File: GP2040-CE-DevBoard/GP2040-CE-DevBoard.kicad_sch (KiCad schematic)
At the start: 0 parts

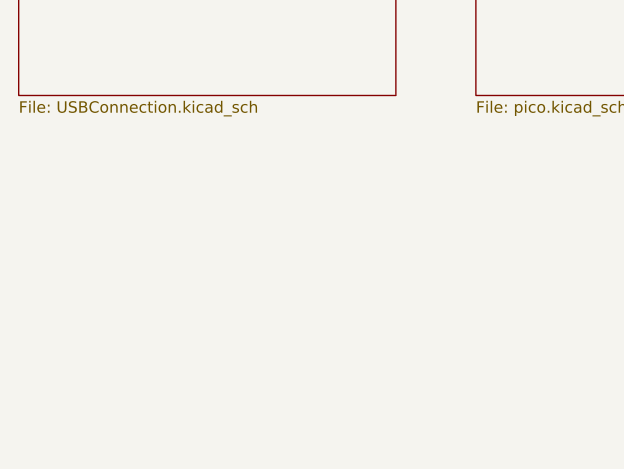
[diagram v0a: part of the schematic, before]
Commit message: Adding Buttons
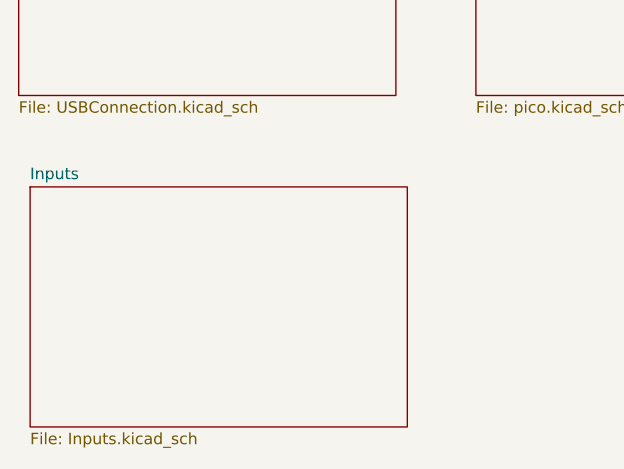
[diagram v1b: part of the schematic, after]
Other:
- added sheet Inputs (Inputs.kicad_sch)
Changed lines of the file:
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@@
+    )
+  )
+  (sheet (at 21.59 59.69) (size 41.91 26.67) (fields_autoplaced)
+    (stroke (width 0.1524) (type solid) (color 0 0 0 0))
+    (fill (color 0 0 0 0.0000))
+    (property "Sheet name" "Inputs" (id 0) (at 21.59 58.9784 0)
+      (effects (font (size 1.27 1.27)) (justify left bottom))
+    )
+    (property "Sheet file" "Inputs.kicad_sch" (id 1) (at 21.59 86.9446 0)
+      (effects (font (size 1.27 1.27)) (justify left top))
     )
   )
@@
     (path "/73fdee15-42f2-4740-b048-36e7f85b9482" (page "3"))
     (path "/b33fe592-84a5-45cc-bdd9-32ad654e4475" (page "4"))
+    (path "/cf4e2c04-ff9e-4c5a-81c6-34ae2464fdd9" (page "5"))
   )
   (symbol_instances
@@
       (reference "#PWR?") (unit 1) (value "GND") (footprint "")
     )
+    (path "/cf4e2c04-ff9e-4c5a-81c6-34ae2464fdd9/49f1f508-92dd-44b5-8cc3-e0cac56a3164"
+      (reference "#PWR?") (unit 1) (value "GND") (footprint "")
+    )
     (path "/b33fe592-84a5-45cc-bdd9-32ad654e4475/4c7c24d6-6d5b-49e6-bf2e-da7d3ae43938"
       (reference "#PWR?") (unit 1) (value "GND") (footprint "")
@@
     )
     (path "/73fdee15-42f2-4740-b048-36e7f85b9482/8d77327b-2bce-4426-8fff-d7f3a5762db8"
+      (reference "#PWR?") (unit 1) (value "GND") (footprint "")
+    )
+    (path "/cf4e2c04-ff9e-4c5a-81c6-34ae2464fdd9/91e16629-9055-4d56-b83e-0a56fc9aee5a"
+      (reference "#PWR?") (unit 1) (value "GND") (footprint "")
+    )
+    (path "/cf4e2c04-ff9e-4c5a-81c6-34ae2464fdd9/9cbedc65-6b48-4c5d-8943-9381607962b6"
       (reference "#PWR?") (unit 1) (value "GND") (footprint "")
     )
@@
       (reference "R?") (unit 1) (value "4.7k") (footprint "Resistor_SMD:R_0805_2012Metric_Pad1.20x1.40mm_HandSolder")
     )
+    (path "/cf4e2c04-ff9e-4c5a-81c6-34ae2464fdd9/0eee3433-e9f7-43cb-b1ae-2be2e9ac6e27"
+      (reference "SW?") (unit 1) (value "SW_Push") (footprint "")
+    )
+    (path "/cf4e2c04-ff9e-4c5a-81c6-34ae2464fdd9/1502c553-9e95-4fe7-a79b-7c0c7eea0150"
+      (reference "SW?") (unit 1) (value "SW_Push") (footprint "")
+    )
+    (path "/cf4e2c04-ff9e-4c5a-81c6-34ae2464fdd9/1ac3d9ce-0481-4d1f-be81-e77269954e3e"
+      (reference "SW?") (unit 1) (value "SW_Push") (footprint "")
+    )
+    (path "/cf4e2c04-ff9e-4c5a-81c6-34ae2464fdd9/24010708-1b23-44d3-b3e1-f95e25bf40d0"
+      (reference "SW?") (unit 1) (value "SW_Push") (footprint "")
+    )
+    (path "/cf4e2c04-ff9e-4c5a-81c6-34ae2464fdd9/31207c80-8b56-4087-bf0b-710dca7763df"
+      (reference "SW?") (unit 1) (value "SW_Push") (footprint "")
+    )
+    (path "/cf4e2c04-ff9e-4c5a-81c6-34ae2464fdd9/3adb4e56-0c30-446e-add9-a441ac4b57cd"
+      (reference "SW?") (unit 1) (value "SW_Push") (footprint "")
+    )
+    (path "/cf4e2c04-ff9e-4c5a-81c6-34ae2464fdd9/42d88e3f-b8f5-411a-b92e-32fb05f43e5f"
+      (reference "SW?") (unit 1) (value "SW_Push") (footprint "")
+    )
+    (path "/cf4e2c04-ff9e-4c5a-81c6-34ae2464fdd9/74ffb43d-c33b-4c8b-abf6-a5ca84fca331"
+      (reference "SW?") (unit 1) (value "SW_Push") (footprint "")
+    )
+    (path "/cf4e2c04-ff9e-4c5a-81c6-34ae2464fdd9/7d9a28b6-31c0-40b8-a6a9-85b90c14eaae"
+      (reference "SW?") (unit 1) (value "SW_Push") (footprint "")
+    )
+    (path "/cf4e2c04-ff9e-4c5a-81c6-34ae2464fdd9/7ee11936-6094-4326-ab0b-c55324458660"
+      (reference "SW?") (unit 1) (value "SW_Push") (footprint "")
+    )
+    (path "/cf4e2c04-ff9e-4c5a-81c6-34ae2464fdd9/8b45d552-607d-4482-8e8b-a9cbdaaf330c"
+      (reference "SW?") (unit 1) (value "SW_Push") (footprint "")
+    )
+    (path "/cf4e2c04-ff9e-4c5a-81c6-34ae2464fdd9/a1ac1f1c-1031-4b49-aaa1-60774ccda8fb"
+      (reference "SW?") (unit 1) (value "SW_Push") (footprint "")
+    )
+    (path "/cf4e2c04-ff9e-4c5a-81c6-34ae2464fdd9/a56d2f31-9696-43af-9213-0c9d4fc4d3b3"
+      (reference "SW?") (unit 1) (value "SW_Push") (footprint "")
+    )
+    (path "/cf4e2c04-ff9e-4c5a-81c6-34ae2464fdd9/a8c128d9-41bc-47f7-bc55-25fd741f1723"
+      (reference "SW?") (unit 1) (value "SW_Push") (footprint "")
+    )
+    (path "/cf4e2c04-ff9e-4c5a-81c6-34ae2464fdd9/acde0591-f8e5-4154-b8e8-d856a642285d"
+      (reference "SW?") (unit 1) (value "SW_Push") (footprint "")
+    )
+    (path "/cf4e2c04-ff9e-4c5a-81c6-34ae2464fdd9/c43176f9-b386-4ff7-b5a3-65697857c04f"
+      (reference "SW?") (unit 1) (value "SW_Push") (footprint "")
+    )
+    (path "/cf4e2c04-ff9e-4c5a-81c6-34ae2464fdd9/f4dbdc93-2160-4f77-bcc7-fead5ea01b99"
+      (reference "SW?") (unit 1) (value "SW_Push") (footprint "")
+    )
+    (path "/cf4e2c04-ff9e-4c5a-81c6-34ae2464fdd9/f676757c-c3bf-4230-bdcd-7dc50df24a95"
+      (reference "SW?") (unit 1) (value "SW_Push") (footprint "")
+    )
+    (path "/cf4e2c04-ff9e-4c5a-81c6-34ae2464fdd9/fa51f695-28f0-4473-baac-b470dfe96665"
+      (reference "SW?") (unit 1) (value "SW_Push") (footprint "")
+    )
+    (path "/cf4e2c04-ff9e-4c5a-81c6-34ae2464fdd9/fbf0d3ff-ce92-42b4-8753-0632c821c353"
+      (reference "SW?") (unit 1) (value "SW_Push") (footprint "")
+    )
+    (path "/cf4e2c04-ff9e-4c5a-81c6-34ae2464fdd9/ffdab74c-ecd0-4aeb-8ce9-af28f040c64e"
+      (reference "SW?") (unit 1) (value "SW_Push") (footprint "")
+    )
     (path "/bd15b165-cf11-4f12-860a-e39af17e96dd/74ad8569-3268-49c3-b75f-a753b79062b4"

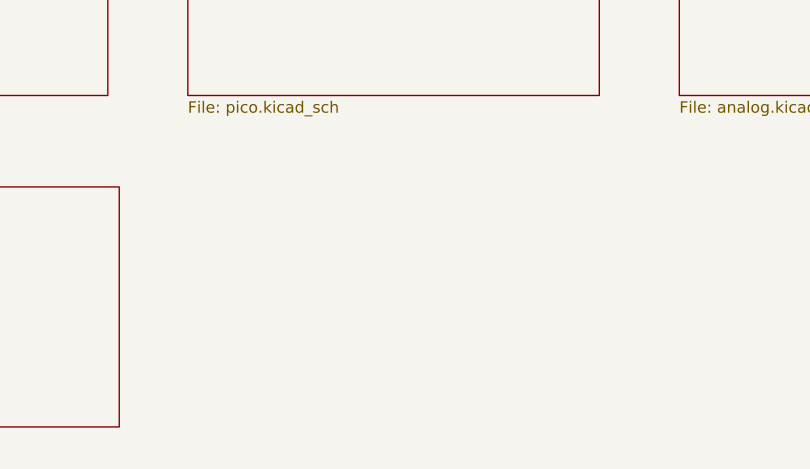
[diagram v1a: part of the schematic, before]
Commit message: Schematic nearly complete, PCB started
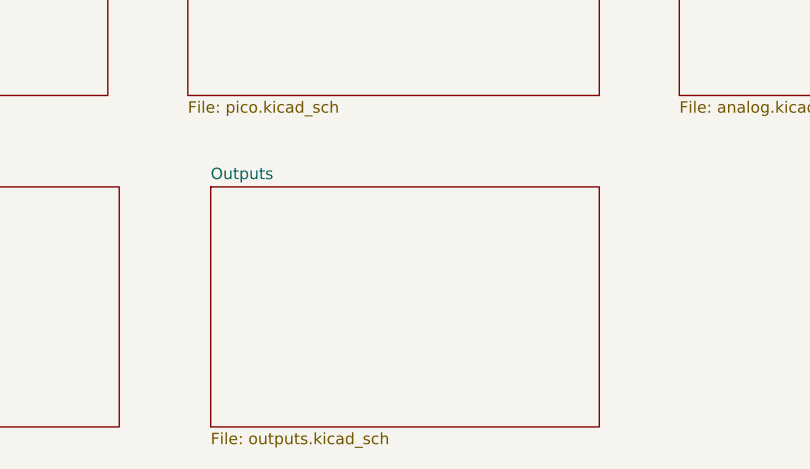
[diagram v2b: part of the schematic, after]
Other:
- added sheet Outputs (outputs.kicad_sch)
